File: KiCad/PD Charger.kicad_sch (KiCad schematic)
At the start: 4 parts, among them J1 USB_C_Receptacle_USB2.0, J3 XT60_M, U7 TPD4E05U06DQA

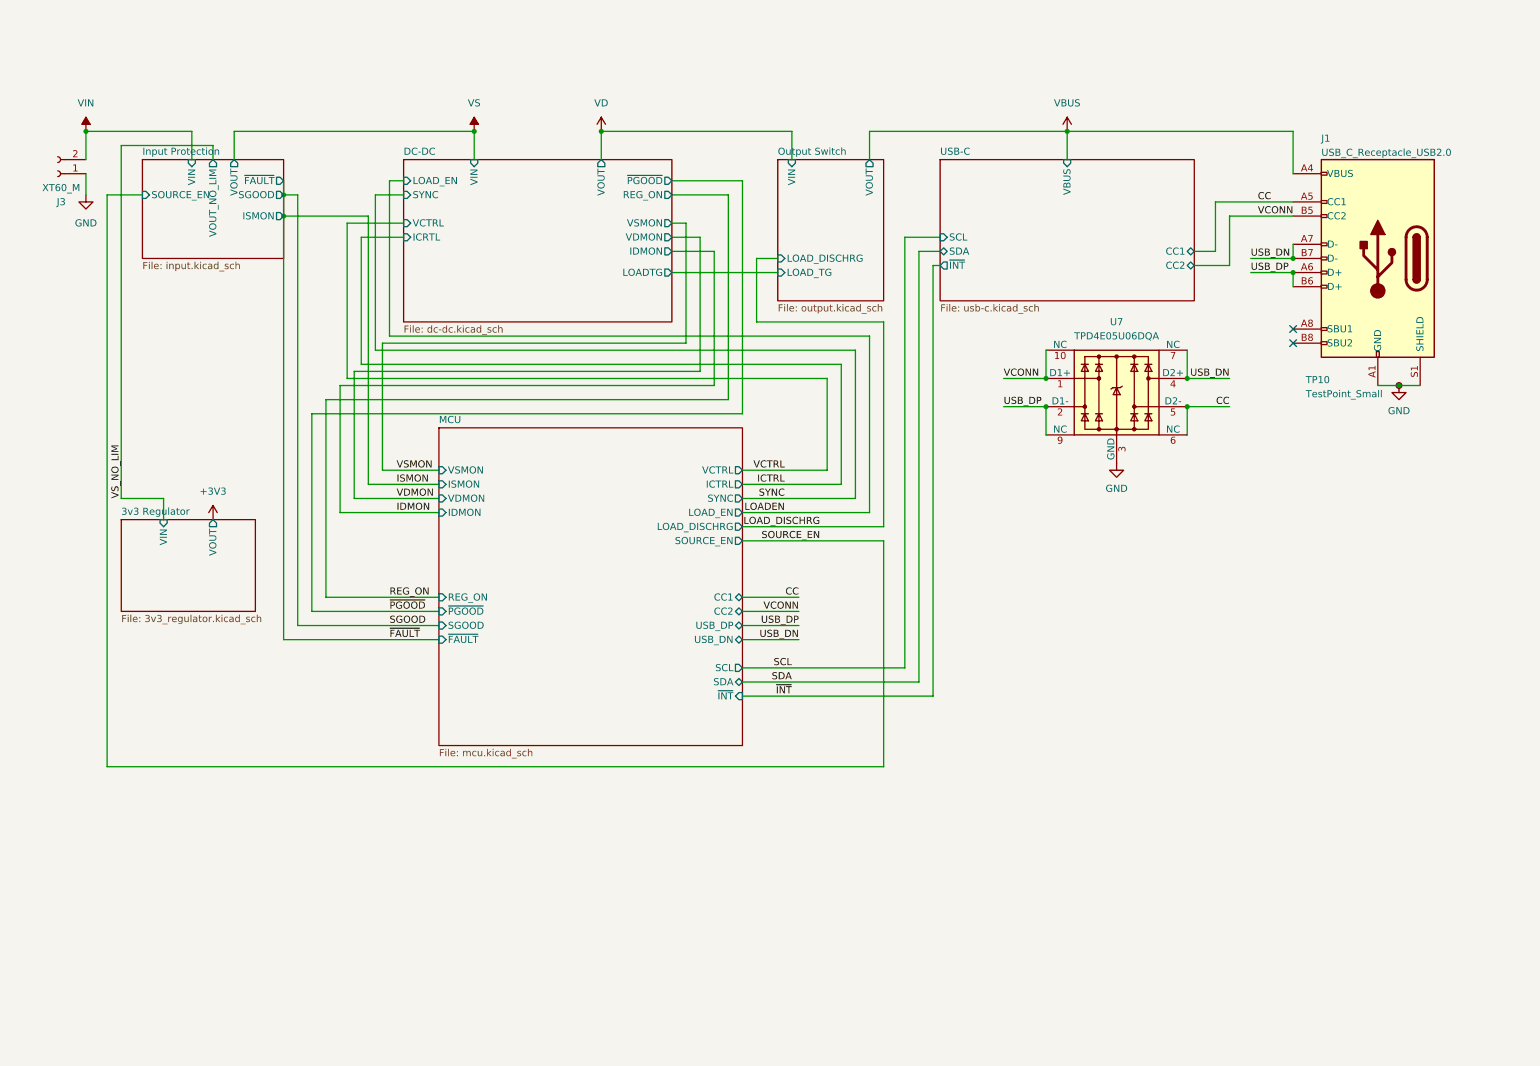
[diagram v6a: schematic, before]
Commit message: standalone regulator core
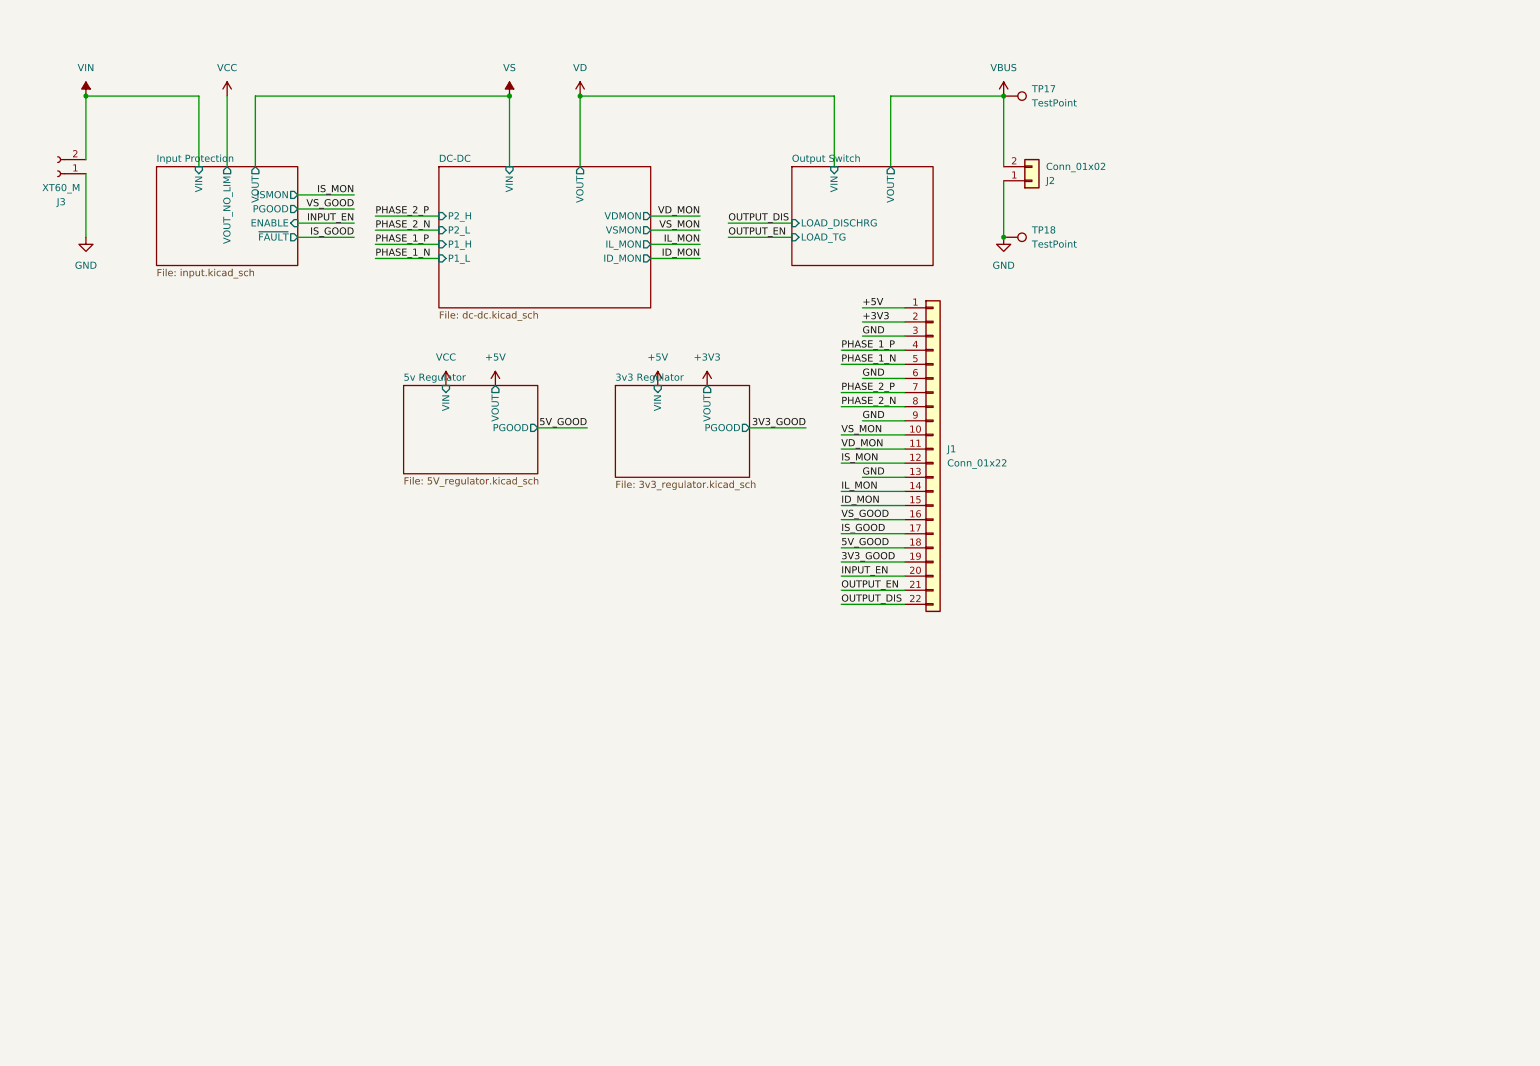
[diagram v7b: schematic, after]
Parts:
- removed J1: USB_C_Receptacle_USB2.0, Connector_USB:USB_C_Receptacle_GCT_USB4105-xx-A_16P_TopMnt_Horizontal, symbol Connector:USB_C_Receptacle_USB2.0
- removed TP10: TestPoint_Small, TestPoint:TestPoint_Pad_D1.0mm, symbol Connector:TestPoint_Small
- removed U7: TPD4E05U06DQA, Package_SON:USON-10_2.5x1.0mm_P0.5mm, symbol Power_Protection:TPD4E05U06DQA
- added J1: Conn_01x22, Connector_PinHeader_2.54mm:PinHeader_1x22_P2.54mm_Vertical, symbol Connector_Generic:Conn_01x22
- added J2: Conn_01x02, Connector_AMASS:AMASS_XT60PW-M_1x02_P7.20mm_Horizontal, symbol Connector_Generic:Conn_01x02
- added TP17, TP18: TestPoint, TestPoint:TestPoint_Keystone_5000-5004_Miniature, symbol Connector:TestPoint
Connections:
- net +3V3: now also J1.2 (Pin_2)
- net GND: now also J1.13 (Pin_13), J1.3 (Pin_3), J1.6 (Pin_6), J1.9 (Pin_9), J2.1 (Pin_1), TP18.1
- net VBUS: now also J2.2 (Pin_2), TP17.1
- new net +5V: J1.1 (Pin_1)
- new net 3V3_GOOD: J1.19 (Pin_19)
- new net 5V_GOOD: J1.18 (Pin_18)
- new net ID_MON: J1.15 (Pin_15)
- new net IL_MON: J1.14 (Pin_14)
- new net INPUT_EN: J1.20 (Pin_20)
- new net IS_GOOD: J1.17 (Pin_17)
- new net IS_MON: J1.12 (Pin_12)
- new net OUTPUT_DIS: J1.22 (Pin_22)
- new net OUTPUT_EN: J1.21 (Pin_21)
- new net PHASE_1_N: J1.5 (Pin_5)
- new net PHASE_1_P: J1.4 (Pin_4)
- new net PHASE_2_N: J1.8 (Pin_8)
- new net PHASE_2_P: J1.7 (Pin_7)
- new net VD_MON: J1.11 (Pin_11)
- new net VS_GOOD: J1.16 (Pin_16)
- new net VS_MON: J1.10 (Pin_10)
- no-connect marks 2 -> 0
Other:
- removed sheet MCU
- removed sheet USB-C
- added sheet 5v Regulator (5V_regulator.kicad_sch)
- sheet 3v3 Regulator ports: added PGOOD; removed none
- sheet DC-DC ports: added ID_MON, IL_MON, P1_H, P1_L, P2_H, P2_L; removed ICRTL, IDMON, LOADTG, LOAD_EN, REG_ON, SYNC, VCTRL, ~{PGOOD}
- sheet Input Protection ports: added ENABLE, PGOOD; removed SGOOD, SOURCE_EN

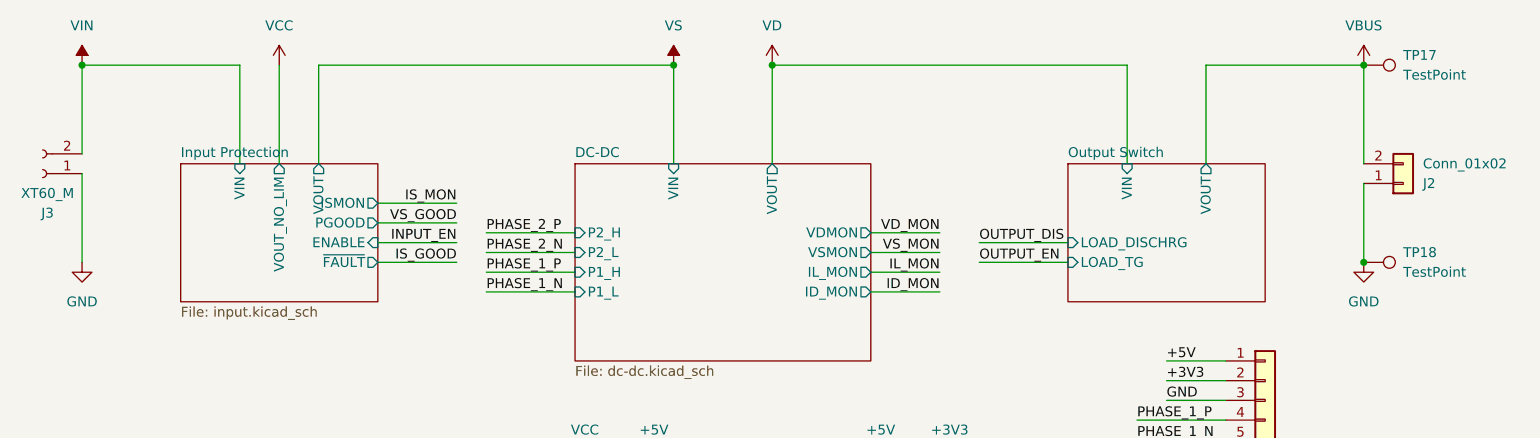
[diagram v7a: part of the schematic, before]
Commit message: 3d models updated
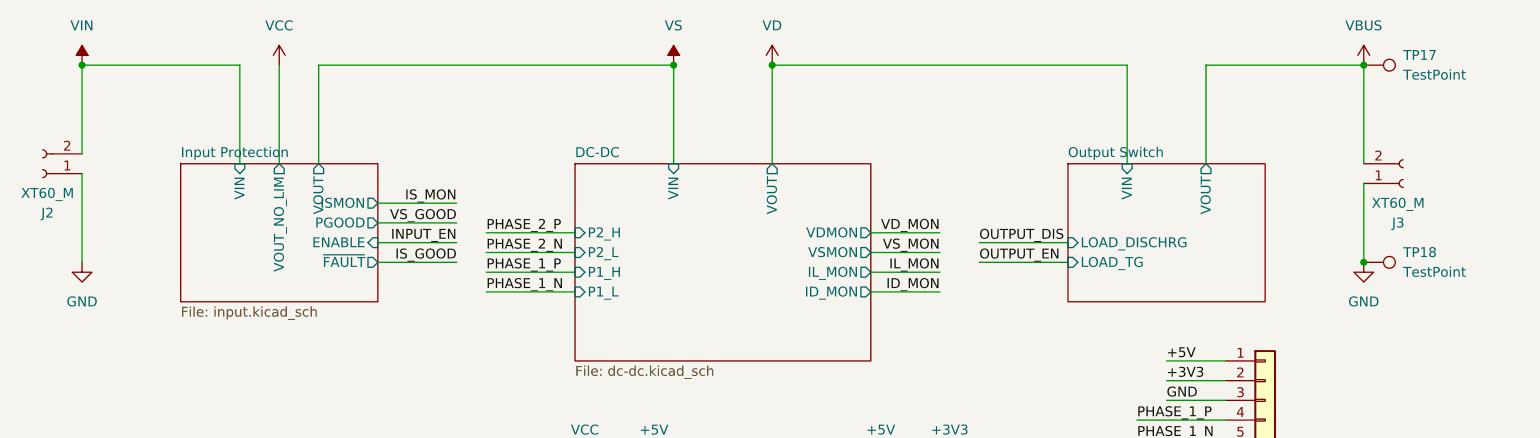
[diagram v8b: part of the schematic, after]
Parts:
- removed J2: Conn_01x02, Connector_AMASS:AMASS_XT60PW-M_1x02_P7.20mm_Horizontal, symbol Connector_Generic:Conn_01x02
- added J3: XT60_M, Connector_AMASS:AMASS_XT60PW-M_1x02_P7.20mm_Horizontal, symbol Connector:Conn_01x02_Socket
- renumbered J3 to J2
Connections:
- net GND: now also J3.1 (Pin_1)
- net VBUS: now also J3.2 (Pin_2)
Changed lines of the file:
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@@
-	)
-	(symbol
-		(lib_id "Connector_Generic:Conn_01x02")
-		(at 195.58 40.64 0)
-		(mirror x)
-		(unit 1)
-		(exclude_from_sim no)
-		(in_bom yes)
-		(on_board yes)
-		(dnp no)
-		(property "Reference" "J2"
-			(at 198.12 40.6401 0)
-			(effects
-				(font
-					(size 1.27 1.27)
-				)
-				(justify left)
-			)
-		)
-		(property "Value" "Conn_01x02"
-			(at 198.12 38.1001 0)
-			(effects
-				(font
-					(size 1.27 1.27)
-				)
-				(justify left)
-			)
-		)
-		(property "Footprint" "Connector_AMASS:AMASS_XT60PW-M_1x02_P7.20mm_Horizontal"
-			(at 195.58 40.64 0)
-			(effects
-				(font
-					(size 1.27 1.27)
-				)
-				(hide yes)
-			)
-		)
-		(property "Datasheet" "~"
-			(at 195.58 40.64 0)
-			(effects
-				(font
-					(size 1.27 1.27)
-				)
-				(hide yes)
-			)
-		)
-		(property "Description" "Generic connector, single row, 01x02, script generated (kicad-library-utils/schlib/autogen/connector/)"
-			(at 195.58 40.64 0)
-			(effects
-				(font
-					(size 1.27 1.27)
-				)
-				(hide yes)
-			)
-		)
-		(pin "2"
-		)
-		(pin "1"
-		)
-		(instances
-			(project ""
-				(path "/2223e2d2-71c8-4f08-b970-c0182a3b98e5"
-					(reference "J2")
-					(unit 1)
-				)
-			)
-		)
 	)
 	(symbol
@@
 		(on_board yes)
 		(dnp no)
-		(property "Reference" "J3"
+		(property "Reference" "J2"
 			(at 20.955 44.45 0)
 			(effects
@@
 			(project "PD Charger"
 				(path "/2223e2d2-71c8-4f08-b970-c0182a3b98e5"
-					(reference "J3")
+					(reference "J2")
 					(unit 1)
 				)
@@
 					(unit 1)
 				)
+			)
+		)
+	)
+	(symbol
+		(lib_id "Connector:Conn_01x02_Socket")
+		(at 195.58 40.64 0)
+		(mirror x)
+		(unit 1)
+		(exclude_from_sim no)
+		(in_bom yes)
+		(on_board yes)
+		(dnp no)
+		(property "Reference" "J3"
+			(at 194.945 45.72 0)
+			(effects
+				(font
+					(size 1.27 1.27)
+				)
+			)
+		)
+		(property "Value" "XT60_M"
+			(at 194.945 43.18 0)
+			(effects
+				(font
+					(size 1.27 1.27)
+				)
+			)
+		)
+		(property "Footprint" "Connector_AMASS:AMASS_XT60PW-M_1x02_P7.20mm_Horizontal"
+			(at 195.58 40.64 0)
+			(effects
+				(font
+					(size 1.27 1.27)
+				)
+				(hide yes)
+			)
+		)
+		(property "Datasheet" "~"
+			(at 195.58 40.64 0)
+			(effects
+				(font
+					(size 1.27 1.27)
+				)
+				(hide yes)
+			)
+		)
+		(property "Description" "Generic connector, single row, 01x02, script generated"
+			(at 195.58 40.64 0)
+			(effects
+				(font
+					(size 1.27 1.27)
+				)
+				(hide yes)
+			)
+		)
+		(pin "1"
+		)
+		(pin "2"
+		)
+		(instances
+			(project "PD Charger"
+				(path "/2223e2d2-71c8-4f08-b970-c0182a3b98e5"
+					(reference "J3")
+					(unit 1)
+				)
